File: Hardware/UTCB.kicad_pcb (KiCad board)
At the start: 2 copper layers, 261 parts, among them IC1 TR05S3V3, J1 NR01105ANG13-2C, J10 Conn_01x06, J2 NR01105ANG13-2C, J3 NR01105ANG13-2C, J4 NR01105ANG13-2C, J5 NR01105ANG13-2C, J6 NR01105ANG13-2C, J7 VXO7805-500-M-TR, J8 3557-2, J9 Conn_01x03, Q1 2SD2653KT146, Q10 2SD2653KT146, Q11 2SD2653KT146, Q12 2SD2653KT146, Q13 2SD2653KT146, Q14 2SD2653KT146, Q15 2SD2653KT146, Q16 2SD2653KT146, Q17 2SD2653KT146, Q18 2SD2653KT146, Q19 2SD2653KT146, Q2 2SD2653KT146, Q20 2SD2653KT146, Q21 2SD2653KT146, Q22 2SD2653KT146, Q23 2SD2653KT146, Q24 2SD2653KT146, Q25 2SD2653KT146, Q26 2SD2653KT146, Q27 2SD2653KT146, Q28 2SD2653KT146, Q29 2SD2653KT146, Q3 2SD2653KT146, Q30 2SD2653KT146, Q31 2SD2653KT146, Q32 2SD2653KT146, Q33 2SD2653KT146, Q34 2SD2653KT146, Q35 2SD2653KT146, Q36 2SD2653KT146, Q37 2SD2653KT146, Q38 2SD2653KT146, Q39 2SD2653KT146, Q4 2SD2653KT146, Q40 2SD2653KT146, Q41 2SD2653KT146, Q42 2SD2653KT146, Q43 2SD2653KT146, Q44 2SD2653KT146, Q45 2SD2653KT146, Q46 2SD2653KT146, Q47 2SD2653KT146, Q48 2SD2653KT146, Q5 2SD2653KT146, Q6 2SD2653KT146, Q7 2SD2653KT146, Q8 2SD2653KT146, Q9 2SD2653KT146

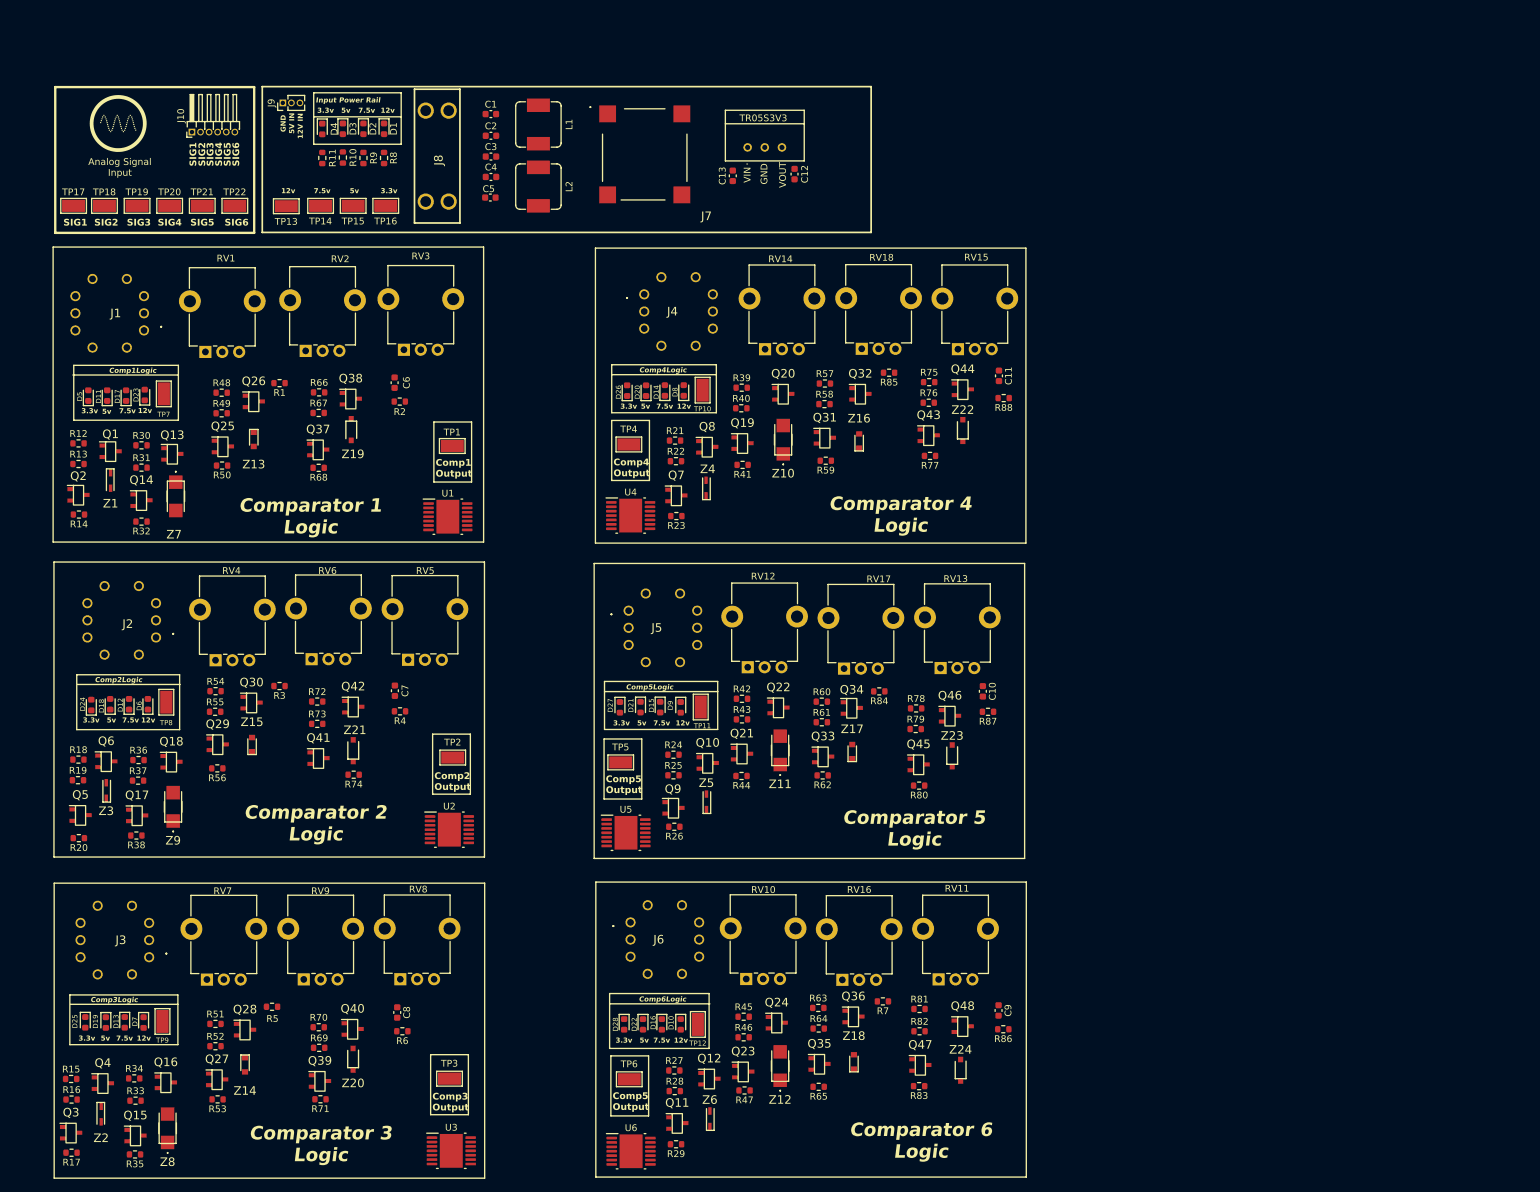
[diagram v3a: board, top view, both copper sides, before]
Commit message: Removed a lot of unnecessary BJT logic, removed rotary switches for logic setting (set all to universal final 3.3v based logic)
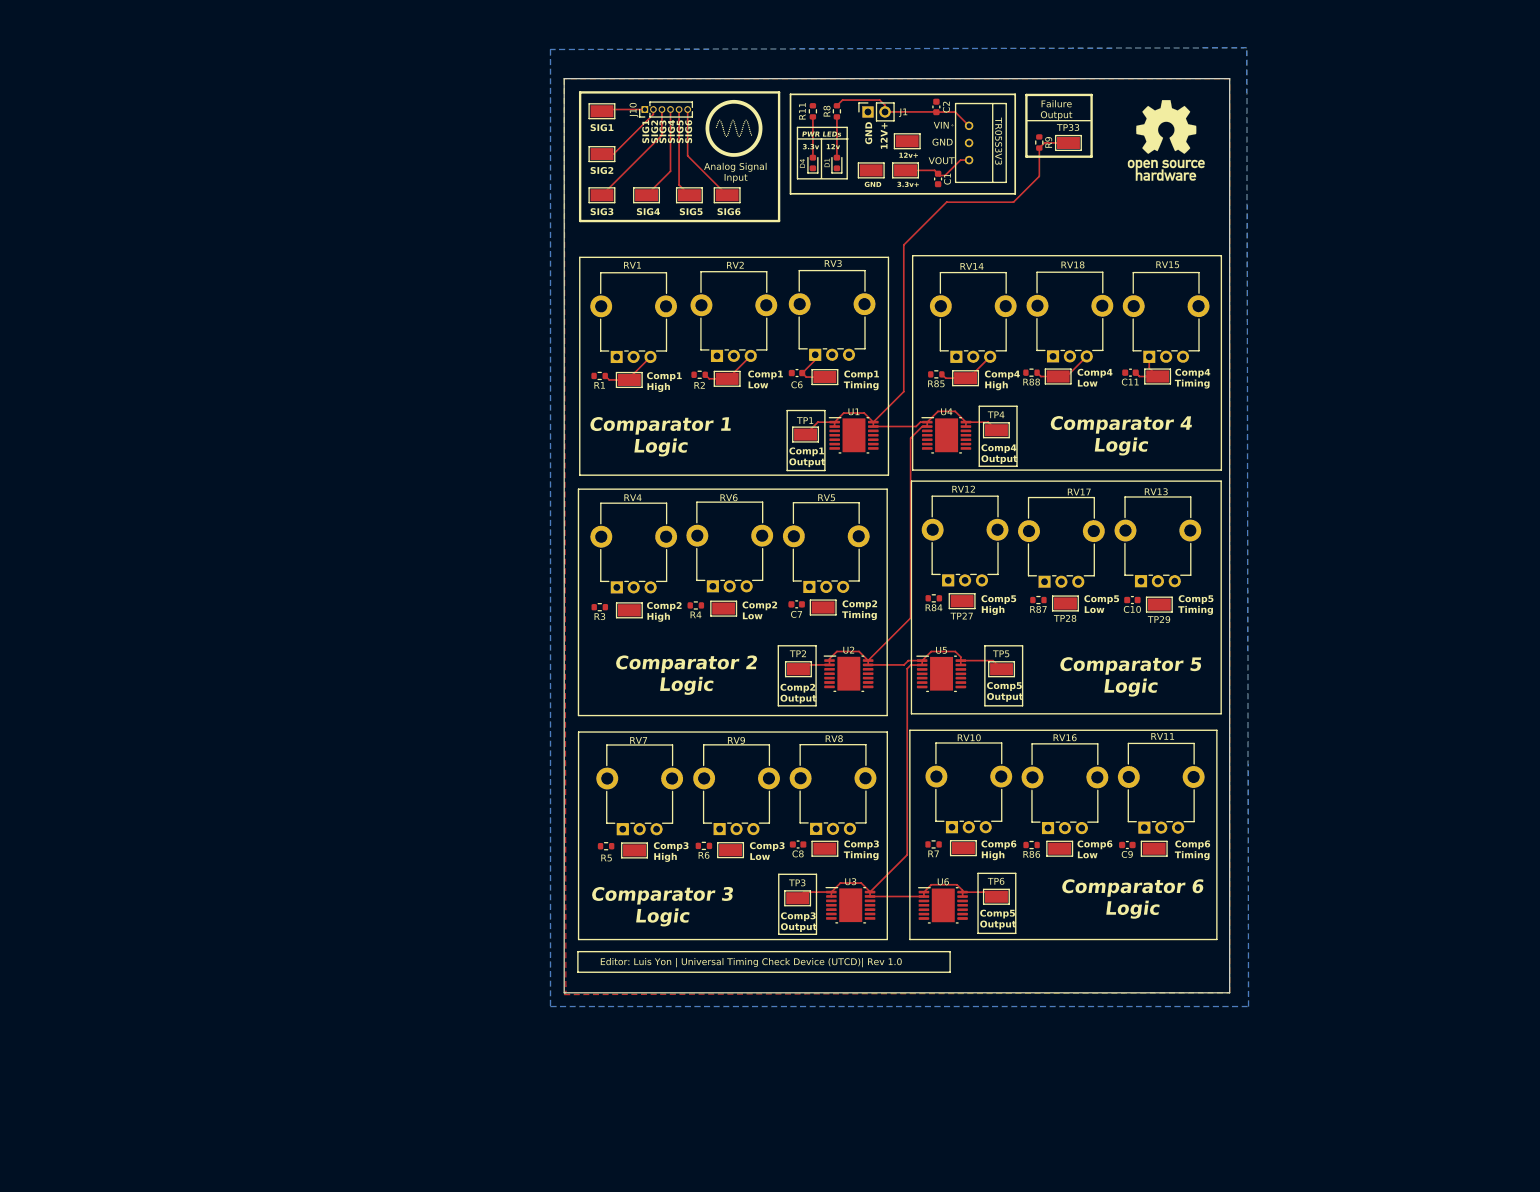
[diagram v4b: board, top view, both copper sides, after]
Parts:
- removed C12: 47uF, Capacitor_SMD:C_0603_1608Metric
- removed C13: 22uF, Capacitor_SMD:C_0603_1608Metric
- removed C3: 10uF, Capacitor_SMD:C_0603_1608Metric
- removed C4: 330uF, Capacitor_SMD:C_0603_1608Metric
- removed C5: C_Small, Capacitor_SMD:C_0603_1608Metric
- removed D10, D5, D6, D7, D8, D9: APT1608SEC/J3-AMT, Diode_SMD:D_0603_1608Metric
- removed D11, D12, D13, D14, D15, D16, D2: APT1608SECK-AMT, Diode_SMD:D_0603_1608Metric
- removed D17, D18, D19, D20, D21, D22, D3: APT1608VRCXF/A-5MAV, Diode_SMD:D_0603_1608Metric
- removed D23, D24, D25, D26, D27, D28: SMLEN3WBC8W1, Diode_SMD:D_0603_1608Metric
- removed J2, J3, J4, J5, J6: NR01105ANG13-2C, Button_Switch_THT:NR01105ANG132C
- removed J7: VXO7805-500-M-TR, Converter_DCDC:VXO7805500MTR
- removed J8: 3557-2, Fuse:3557-2
- removed J9: Conn_01x03, Connector_PinHeader_1.27mm:PinHeader_1x03_P1.27mm_Vertical
- removed L1: 82uH, Inductor_SMD:L_Sumida_CDMC6D28_7.25x6.5mm
- removed L2: 22uH, Inductor_SMD:L_Sumida_CDMC6D28_7.25x6.5mm
- removed Q1, Q10, Q11, Q12, Q13, Q14, Q15, Q16, Q17, Q18, Q19, Q2, Q20, Q21, Q22, Q23, Q24, Q25, Q26, Q27, Q28, Q29, Q3, Q30, Q31, Q32, Q33, Q34, Q35, Q36, Q37, Q38, Q39, Q4, Q40, Q41, Q42, Q43, Q44, Q45, Q46, Q47, Q48, Q5, Q6, Q7, Q8, Q9: 2SD2653KT146, Package_TO_SOT_SMD:SOT85P240X115-3N
- removed R10: R_Small, Resistor_SMD:R_0603_1608Metric
- removed R12, R15, R18, R21, R24, R27, R30, R33, R36, R39, R42, R45, R48, R51, R54, R57, R60, R63, R66, R69, R72, R75, R78, R81: 1kΩ, Resistor_SMD:R_0603_1608Metric
- removed R13, R16, R19, R22, R25, R28, R31, R34, R37, R40, R43, R46, R49, R52, R55, R58, R61, R64, R67, R70, R73, R76, R79, R82: 4.7kΩ, Resistor_SMD:R_0603_1608Metric
- removed R14, R17, R20, R23, R26, R29, R32, R35, R38, R41, R44, R47, R50, R53, R56, R59, R62, R65, R68, R71, R74, R77, R80, R83: 565 Ω, Resistor_SMD:R_0603_1608Metric
- removed Z1, Z2, Z3, Z4, Z5, Z6: MM3Z12VT1GX, Diode_SMD:SOD2512X110N
- removed Z10, Z11, Z12, Z7, Z8, Z9: PTZTFTE257.5B, Diode_SMD:PTZTFTE2575B
- removed Z13, Z14, Z15, Z16, Z17, Z18: UDZVTE-174.7B, Diode_SMD:UDZVTE1722B
- removed Z19, Z20, Z21, Z22, Z23, Z24: BZT52H-A3V3-QX, Diode_SMD:SODFL3516X120N
- added REF**: OSHW-Logo_11.4x12mm_SilkScreen, Symbol:OSHW-Logo_11.4x12mm_SilkScreen, F.Cu at (185.9, 30.7)
- added TP23: COMP3_TIMING, TestPoint:TestPoint_Keystone_5015_Micro-Minature, F.Cu at (135.4, 135.6)
- added TP24: COMP4_HIGH, TestPoint:TestPoint_Keystone_5015_Micro-Minature, F.Cu at (156.2, 66.0)
- added TP25: COMP4_HIGH, TestPoint:TestPoint_Keystone_5015_Micro-Minature, F.Cu at (169.9, 65.7)
- added TP26: COMP4_TIMING, TestPoint:TestPoint_Keystone_5015_Micro-Minature, F.Cu at (184.7, 65.7)
- added TP27: COMP5_HIGH, TestPoint:TestPoint_Keystone_5015_Micro-Minature, F.Cu at (155.7, 99.0)
- added TP28: COMP5_HIGH, TestPoint:TestPoint_Keystone_5015_Micro-Minature, F.Cu at (171.0, 99.3)
- added TP29: COMP3_TIMING, TestPoint:TestPoint_Keystone_5015_Micro-Minature, F.Cu at (184.9, 99.5)
- added TP30: COMP6_HIGH, TestPoint:TestPoint_Keystone_5015_Micro-Minature, F.Cu at (155.9, 135.5)
- added TP31: COMP6_HIGH, TestPoint:TestPoint_Keystone_5015_Micro-Minature, F.Cu at (170.2, 135.6)
- added TP32: COMP6_TIMING, TestPoint:TestPoint_Keystone_5015_Micro-Minature, F.Cu at (184.2, 135.6)
- added TP33: Failure_Check, TestPoint:TestPoint_Keystone_5015_Micro-Minature, F.Cu at (171.4, 31.1)
- added TP34: GND_Check, TestPoint:TestPoint_Keystone_5015_Micro-Minature, F.Cu at (142.2, 35.2)
- C1: value 330uF -> 47uF
- C2: value 10uF -> 22uF
- J1: value NR01105ANG13-2C -> Conn_01x02; footprint Button_Switch_THT:NR01105ANG132C -> Connector_PinSocket_2.54mm:PinSocket_1x02_P2.54mm_Vertical
- J10: footprint Connector_PinHeader_1.27mm:PinHeader_1x06_P1.27mm_Horizontal -> Connector_PinHeader_1.27mm:PinHeader_1x06_P1.27mm_Vertical
- R9: value R_Small -> 1k
- TP10: value Comp4_Logic -> COMP2_HIGH
- TP11: value Comp5_Logic -> COMP2_LOW
- TP12: value Comp6_Logic -> COMP2_TIMING
- TP14: value 7.5v_Check -> COMP3_HIGH
- TP15: value 5v_Check -> COMP3_HIGH
- TP7: value Comp1_Logic -> COMP1_HIGH
- TP8: value Comp2_Logic -> COMP1_LOW
- TP9: value Comp3_Logic -> COMP1_TIMING
- moved TP9 136.9 mm to (135.4, 65.8), turned to 180 degrees
- moved J1 112.0 mm to (141.8, 26.5), turned to 90 degrees
- moved TP15 110.6 mm to (121.4, 135.8), turned to 180 degrees
- moved TP14 106.2 mm to (107.2, 135.9), turned to 180 degrees
- moved R9 100.1 mm to (167.1, 31.1)
- moved TP8 95.9 mm to (120.9, 66.0), turned to 180 degrees
- moved TP13 92.5 mm to (147.6, 30.9)
- moved G*** 91.2 mm to (121.9, 29.0)
- moved TP17 79.5 mm to (102.4, 26.4)
- moved TP16 77.2 mm to (147.3, 35.2)
- moved TP18 74.1 mm to (102.4, 32.8)
- moved R11 73.0 mm to (133.6, 26.4), turned to -90 degrees
- moved TP22 72.9 mm to (120.9, 38.9)
- moved D4 72.8 mm to (133.6, 34.1), turned to 90 degrees
- moved TP21 72.2 mm to (115.3, 38.9)
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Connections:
- C1 pad 1: Net-(C1-Pad1) -> +3.3V
- C2 pad 1: Net-(C2-Pad1) -> +12V
- J1 pad 1: +12V -> GND
- J1 pad 2: +7.5V -> +12V
- R9 pad 1: Net-(D2-A) -> +3.3V
- R9 pad 2: +7.5V -> COMP1A
- RV1 pad 1: SetComparator1Logic -> +3.3V
- RV10 pad 1: SetComparator6Logic -> +3.3V
- RV12 pad 1: SetComparator5Logic -> +3.3V
- RV14 pad 1: SetComparator4Logic -> +3.3V
- RV16 pad 1: SetComparator6Logic -> +3.3V
- RV17 pad 1: SetComparator5Logic -> +3.3V
- RV18 pad 1: SetComparator4Logic -> +3.3V
- RV2 pad 1: SetComparator1Logic -> +3.3V
- RV4 pad 1: SetComparator2Logic -> +3.3V
- RV6 pad 1: SetComparator2Logic -> +3.3V
- RV7 pad 1: SetComparator3Logic -> +3.3V
- RV9 pad 1: SetComparator3Logic -> +3.3V
- TP10 pad 1: SetComparator4Logic -> /ComparatorLogic/COMP2_HIGH
- TP11 pad 1: SetComparator5Logic -> /ComparatorLogic/COMP2_LOW
- TP12 pad 1: SetComparator6Logic -> /ComparatorLogic/Timing2Check
- TP14 pad 1: +7.5V -> /ComparatorLogic/COMP3_HIGH
- TP15 pad 1: +5V -> /ComparatorLogic/COMP3_LOW
- TP2 pad 1: COMP2A -> COMP1A
- TP3 pad 1: COMP3A -> COMP1A
- TP4 pad 1: COMP4A -> COMP1A
- TP5 pad 1: COMP5A -> COMP1A
- TP6 pad 1: COMP6A -> COMP1A
- TP7 pad 1: SetComparator1Logic -> /ComparatorLogic/COMP1_HIGH
- TP8 pad 1: SetComparator2Logic -> /ComparatorLogic/COMP1_LOW
- TP9 pad 1: SetComparator3Logic -> /ComparatorLogic/Timing1Check
- U1 pad 3: SetComparator1Logic -> +3.3V
- U2 pad 1: COMP5A -> COMP1A
- U2 pad 13: COMP5A -> COMP1A
- U2 pad 14: COMP5A -> COMP1A
- U2 pad 2: COMP5A -> COMP1A
- U2 pad 3: SetComparator5Logic -> +3.3V
- U2 pad 4: unconnected-(U2-1IN--Pad4) -> Signal2
- U2 pad 5: unconnected-(U2-1IN+-Pad5) -> /ComparatorLogic/COMP2_HIGH
- U2 pad 6: unconnected-(U2-2IN--Pad6) -> /ComparatorLogic/COMP2_LOW
- U2 pad 7: unconnected-(U2-2IN+-Pad7) -> Signal2
- U2 pad 8: unconnected-(U2-3IN+-Pad8) -> /ComparatorLogic/Timing2Check
- U3 pad 1: COMP3A -> COMP1A
- U3 pad 13: COMP3A -> COMP1A
- U3 pad 14: COMP3A -> COMP1A
- U3 pad 2: COMP3A -> COMP1A
- U3 pad 3: SetComparator3Logic -> +3.3V
- U4 pad 1: COMP4A -> COMP1A
- U4 pad 13: COMP4A -> COMP1A
- U4 pad 14: COMP4A -> COMP1A
- U4 pad 2: COMP4A -> COMP1A
- U4 pad 3: SetComparator4Logic -> +3.3V
- U5 pad 1: COMP5A -> COMP1A
- U5 pad 13: COMP5A -> COMP1A
- U5 pad 14: COMP5A -> COMP1A
- U5 pad 2: COMP5A -> COMP1A
- U5 pad 3: SetComparator5Logic -> +3.3V
- U6 pad 1: COMP6A -> COMP1A
- U6 pad 13: COMP6A -> COMP1A
- U6 pad 14: COMP6A -> COMP1A
- U6 pad 2: COMP6A -> COMP1A
- U6 pad 3: SetComparator6Logic -> +3.3V
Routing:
- net COMP1A: track 0.00 -> 243.9 mm
- net +12V: track 0.00 -> 22.1 mm
- net Signal3: track 0.00 -> 16.4 mm
- net Signal6: track 0.00 -> 15.1 mm
- net Signal4: track 0.00 -> 14.2 mm
- net Signal5: track 0.00 -> 13.3 mm
- net Signal2: track 0.00 -> 10.8 mm
- net +3.3V: track 0.00 -> 10.7 mm
- net /ComparatorLogic/COMP4_LOW: track 0.00 -> 8.83 mm
- net /ComparatorLogic/COMP4_HIGH: track 0.00 -> 8.70 mm
- net /ComparatorLogic/COMP1_HIGH: track 0.00 -> 8.52 mm
- net /ComparatorLogic/COMP1_LOW: track 0.00 -> 8.39 mm
- net /ComparatorLogic/Timing1Check: track 0.00 -> 7.11 mm
- net /ComparatorLogic/Timing4Check: track 0.00 -> 6.92 mm
- net Signal1: track 0.00 -> 6.46 mm
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- added copper zone on In2.Cu, net +3.3V
- added copper zone on B.Cu, net GND
- added copper zone on F.Cu, net GND
- added copper zone on In1.Cu, net GND
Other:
- board outline added: 98.6 x 135.4 mm
- copper layers 2 -> 4
- board text added: "12V+"
- board text added: "12v+"
- board text added: "3.3v+"
- board text added: "Comp1 High"
- board text added: "Comp1 Low"
- board text added: "Comp1 Timing"
- board text added: "Comp2 High"
- board text added: "Comp2 Low"
- board text added: "Comp2 Timing"
- board text added: "Comp3 High"
- board text added: "Comp3 Low"
- board text added: "Comp3 Timing"
- board text added: "Comp4 High"
- board text added: "Comp4 Low"
- board text added: "Comp4 Timing"
- board text added: "Comp5 High"
- board text added: "Comp5 Low"
- board text added: "Comp5 Timing"
- board text added: "Comp6 High"
- board text added: "Comp6 Low"
- board text added: "Comp6 Timing"
- board text added: "Editor: Luis Yon | Universal Timing Check Device (UTCD)| Rev 1.0"
- board text added: "Failure Output"
- board text added: "PWR LEDs"
- board text removed: "12V IN"
- board text removed: "5V IN"
- board text removed: "5v"
- board text removed: "7.5v"
- board text removed: "Comp1Logic"
- board text removed: "Comp2Logic"
- board text removed: "Comp3Logic"
- board text removed: "Comp4Logic"
- board text removed: "Comp5Logic"
- board text removed: "Comp6Logic"
- board text removed: "Input Power Rail"

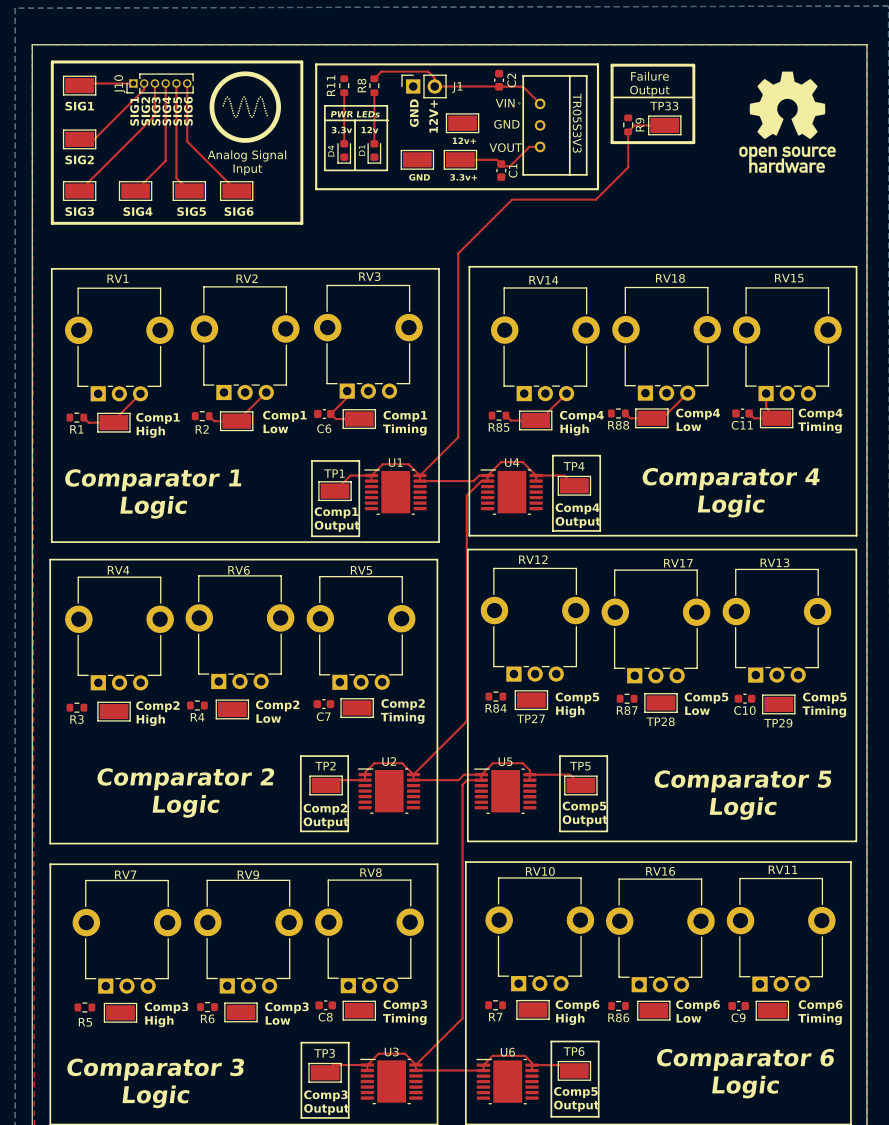
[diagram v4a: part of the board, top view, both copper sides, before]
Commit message: Added dip switch for comparator active selection
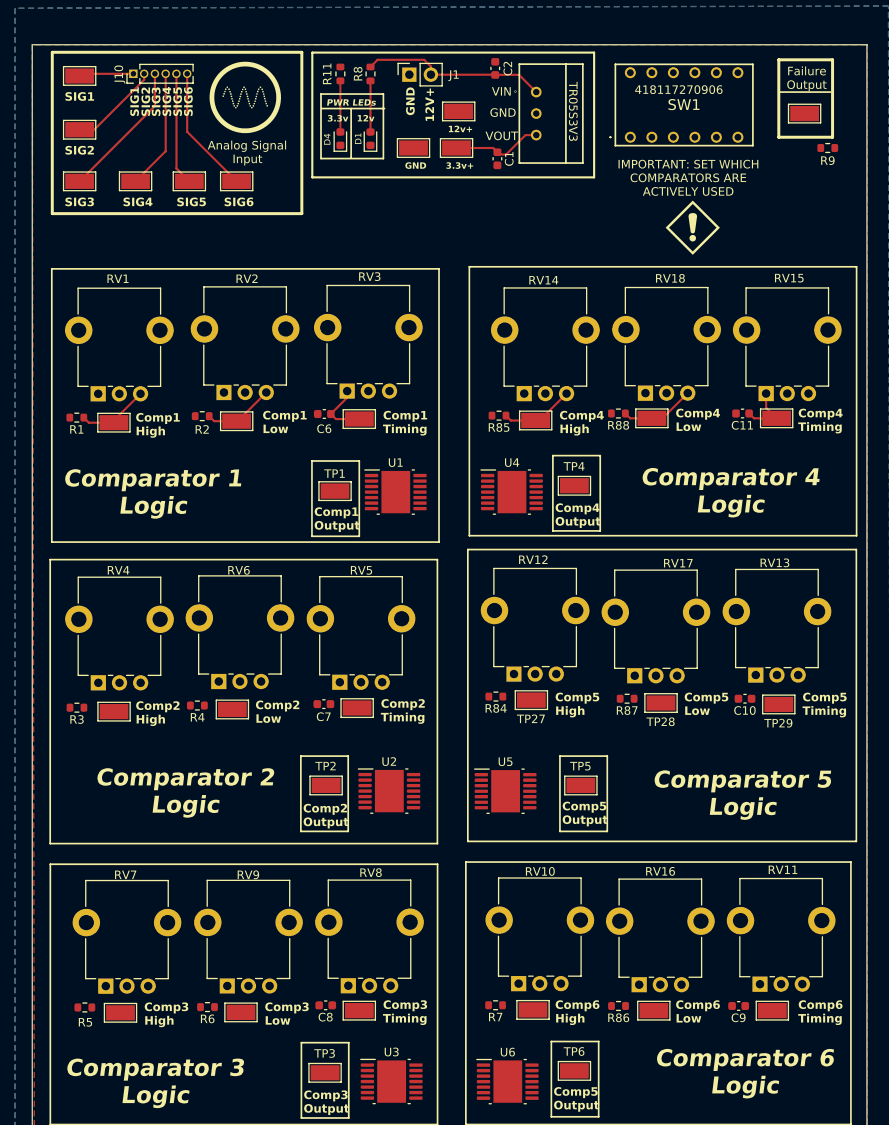
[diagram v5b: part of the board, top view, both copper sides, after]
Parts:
- removed REF**: OSHW-Logo_11.4x12mm_SilkScreen, Symbol:OSHW-Logo_11.4x12mm_SilkScreen
- added G***: LOGO, Symbol:HazardSymbol, F.Cu at (174.8, 43.2)
- added SW1: SW_DIP_x06, Button_Switch_THT:418117270906, F.Cu at (167.4, 32.5)
- moved R9 23.7 mm to (190.7, 33.8), turned to 180 degrees
- moved TP33 16.6 mm to (188.0, 29.7)
- moved C2 1.47 mm to (151.4, 24.4)
- moved IC1 1.47 mm to (154.3, 29.7)
- moved J1 1.47 mm to (141.3, 25.1)
- moved TP13 1.47 mm to (147.1, 29.5)
- moved TP16 1.47 mm to (146.9, 33.8)
- moved TP34 1.47 mm to (141.8, 33.8)
- moved R11 1.47 mm to (133.1, 25.0)
- moved R8 1.47 mm to (136.7, 25.0)
- moved D1 1.47 mm to (136.7, 32.7)
- moved D4 1.47 mm to (133.1, 32.7)
- moved C1 1.47 mm to (151.7, 35.1)
- moved G*** 1.14 mm to (121.9, 27.8)
- moved J10 1.14 mm to (108.7, 25.0)
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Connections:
- R9 pad 2: COMP1A -> /ComparatorLogic/Failure_Output
- TP2 pad 1: COMP1A -> COMP2A
- TP3 pad 1: COMP1A -> COMP3A
- TP33 pad 1: COMP1A -> /ComparatorLogic/Failure_Output
- TP4 pad 1: COMP1A -> COMP4A
- TP5 pad 1: COMP1A -> COMP5A
- TP6 pad 1: COMP1A -> COMP6A
- U2 pad 1: COMP1A -> COMP2A
- U2 pad 13: COMP1A -> COMP2A
- U2 pad 14: COMP1A -> COMP2A
- U2 pad 2: COMP1A -> COMP2A
- U3 pad 1: COMP1A -> COMP3A
- U3 pad 13: COMP1A -> COMP3A
- U3 pad 14: COMP1A -> COMP3A
- U3 pad 2: COMP1A -> COMP3A
- U4 pad 1: COMP1A -> COMP4A
- U4 pad 13: COMP1A -> COMP4A
- U4 pad 14: COMP1A -> COMP4A
- U4 pad 2: COMP1A -> COMP4A
- U5 pad 1: COMP1A -> COMP5A
- U5 pad 13: COMP1A -> COMP5A
- U5 pad 14: COMP1A -> COMP5A
- U5 pad 2: COMP1A -> COMP5A
- U6 pad 1: COMP1A -> COMP6A
- U6 pad 13: COMP1A -> COMP6A
- U6 pad 14: COMP1A -> COMP6A
- U6 pad 2: COMP1A -> COMP6A
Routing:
- net COMP1A: track 243.9 -> 0.00 mm
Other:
- board text added: "IMPORTANT: SET WHICH COMPARATORS ARE ACTIVELY USED"
